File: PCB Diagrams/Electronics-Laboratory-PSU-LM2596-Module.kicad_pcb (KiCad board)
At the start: 2 copper layers, 74.9 x 49.5 mm, 17 parts, among them J1 Bornier 01x02, J10 Conn_01x03, J11 Conn_01x02, J12 Conn_01x01, J2 Bornier 01x02, J3 Conn_01x01, J4 Conn_01x01, J5 Conn_01x01, J6 Conn_01x01, J7 Conn_01x03, J8 Conn_01x03, J9 Conn_01x03

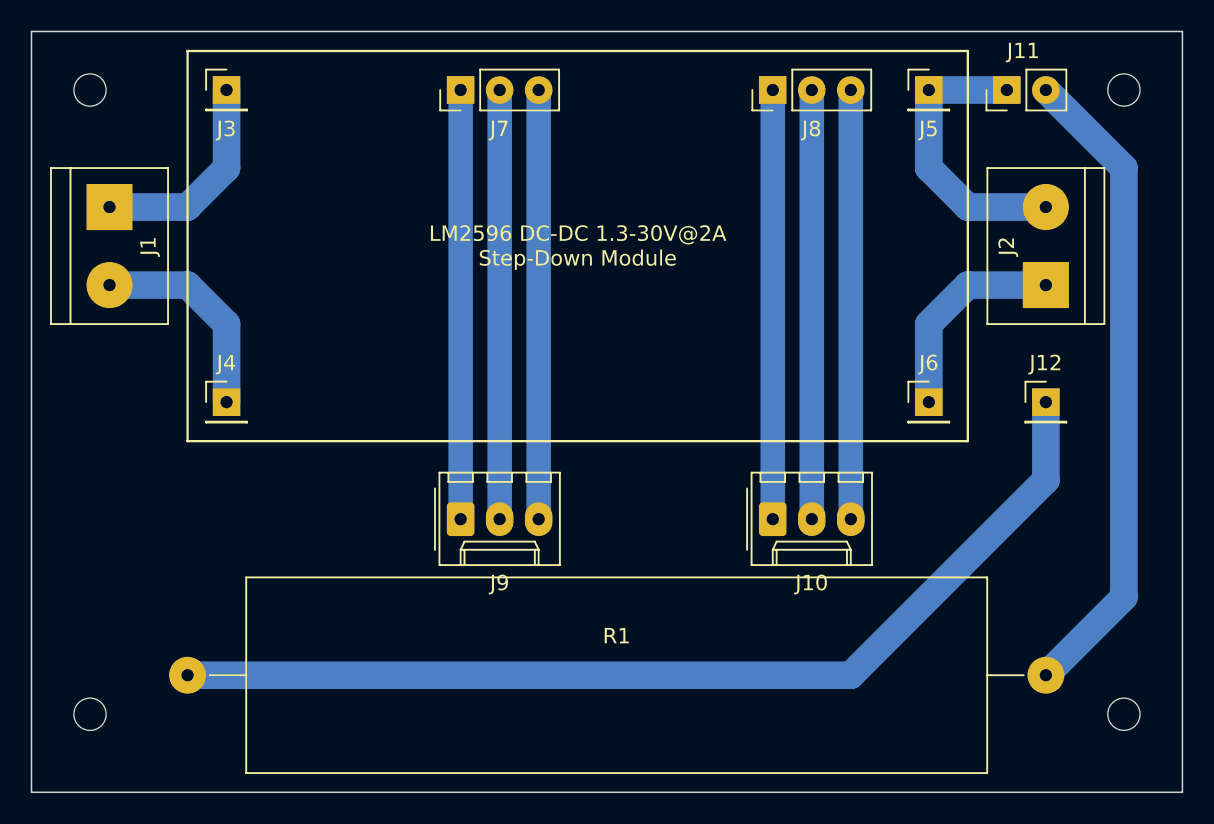
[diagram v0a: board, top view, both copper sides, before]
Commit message: update electronic diagrams, adding case 3D model
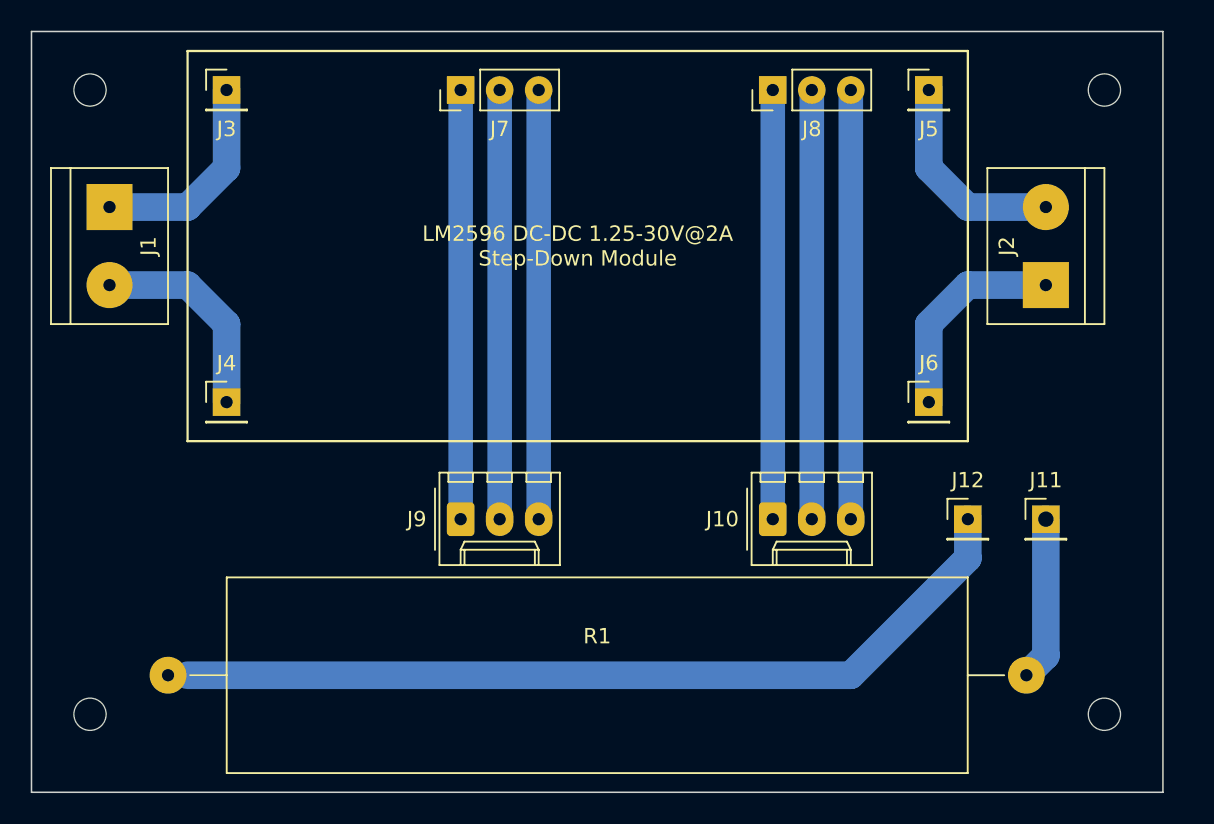
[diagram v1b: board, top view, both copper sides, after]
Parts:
- J1, J2: value Bornier 01x02 -> Bornier x02
- J10: value Conn_01x03 -> Current Pot.
- J11: value Conn_01x02 -> SWITCH; footprint Connector_PinHeader_2.54mm:PinHeader_1x02_P2.54mm_Vertical -> Connector_PinHeader_2.54mm:PinHeader_1x01_P2.54mm_Vertical
- J12: value Conn_01x01 -> AMP.
- J3: value Conn_01x01 -> Module IN+
- J4: value Conn_01x01 -> Module IN-
- J5: value Conn_01x01 -> Module OUT+
- J6: value Conn_01x01 -> Module OUT-
- J7, J8: value Conn_01x03 -> Conn x03
- J9: value Conn_01x03 -> Volt Pot.
- moved R1 57.1 mm to (118.1, 114.3), turned to 0 degrees
- moved J11 28.1 mm to (175.3, 104.1), turned to 0 degrees
- moved J12 9.16 mm to (170.2, 104.1)
- moved H2 1.27 mm to (179.1, 76.2)
- moved H3 1.27 mm to (179.1, 116.8)
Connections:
- J11 pad 1: +VDC -> Net-(J11-Pad1)
- R1 pad 1: Net-(J11-Pad2) -> Net-(J12-Pad1)
- R1 pad 2: Net-(J12-Pad1) -> Net-(J11-Pad1)
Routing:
- net Net-(J11-Pad2): track 42.3 -> 0.00 mm
- net Net-(J11-Pad1): track 0.00 -> 10.7 mm
- net Net-(J12-Pad1): track 66.2 -> 56.5 mm
- net +VDC: track 18.8 -> 13.8 mm
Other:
- board size 74.9 x 49.5 mm -> 73.7 x 49.5 mm
- board text added: "LM2596 DC-DC 1.25-30V@2A Step-Down Module"
- board text removed: "LM2596 DC-DC 1.3-30V@2A Step-Down Module"
